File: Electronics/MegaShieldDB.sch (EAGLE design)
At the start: 45 parts, among them IC2 MCP4802, IC3 MCP4802, IC4 4013N, Q1 BF199, Q5 BF199, X1 Panel, X2 Cruise, X3 Motor, X4 Steer, X5 Brake

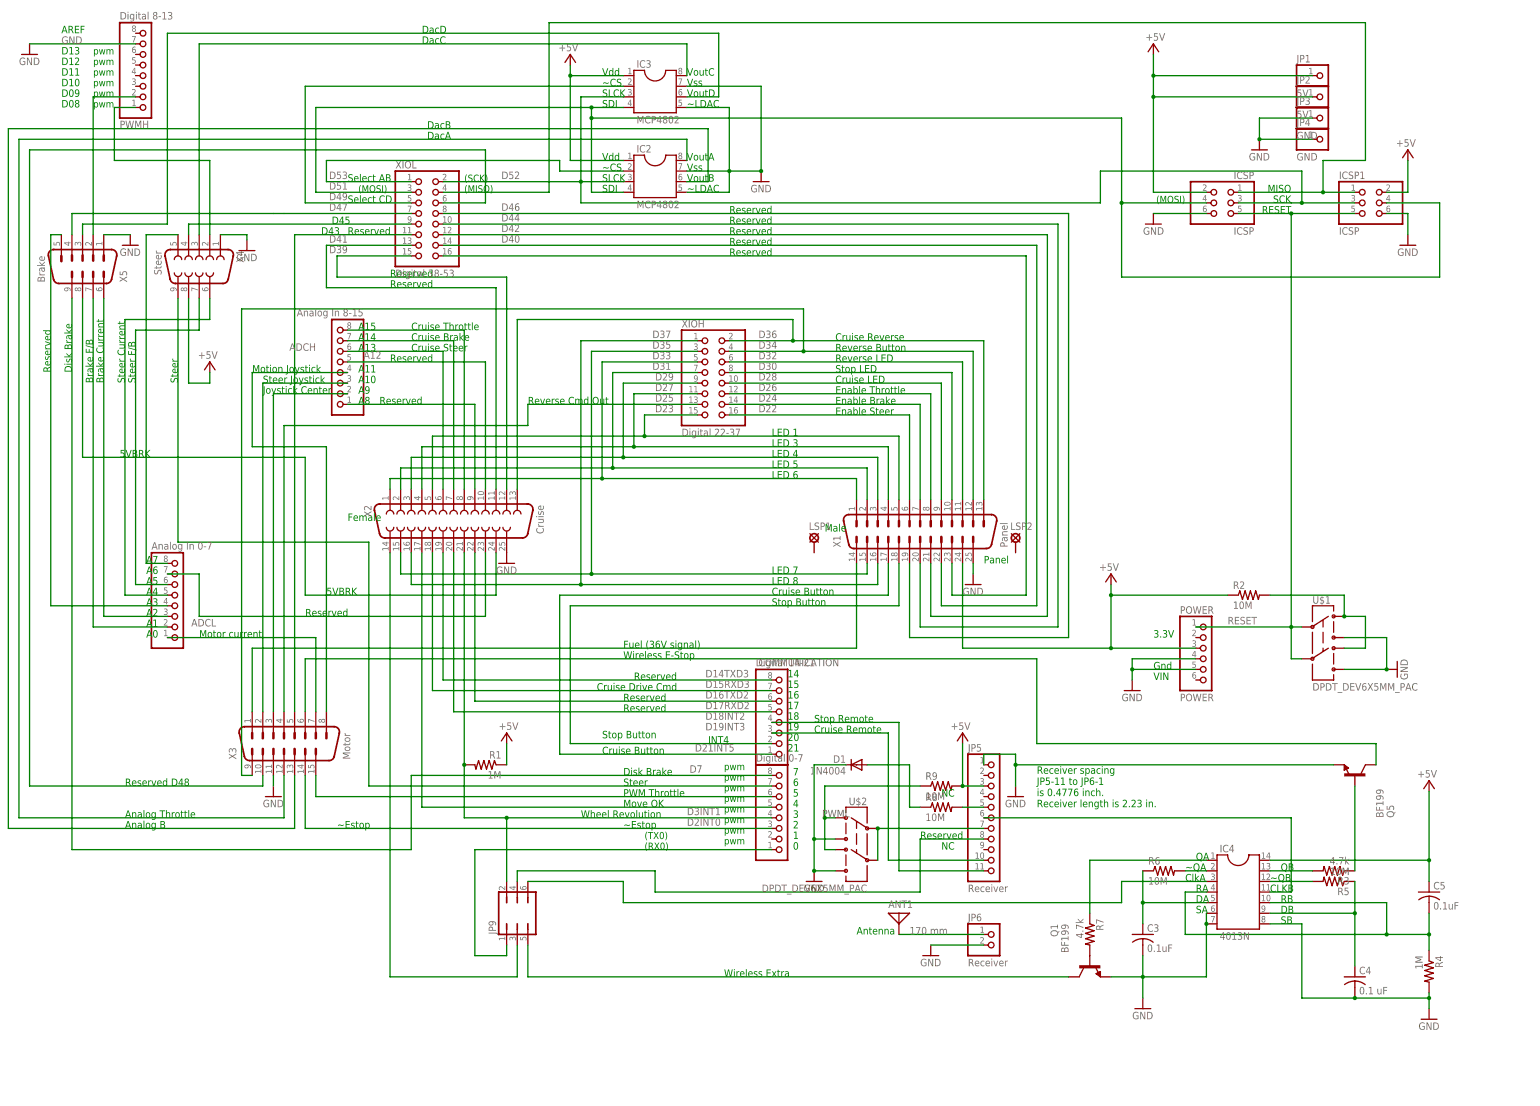
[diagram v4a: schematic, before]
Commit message: Routed with thick power and ground.
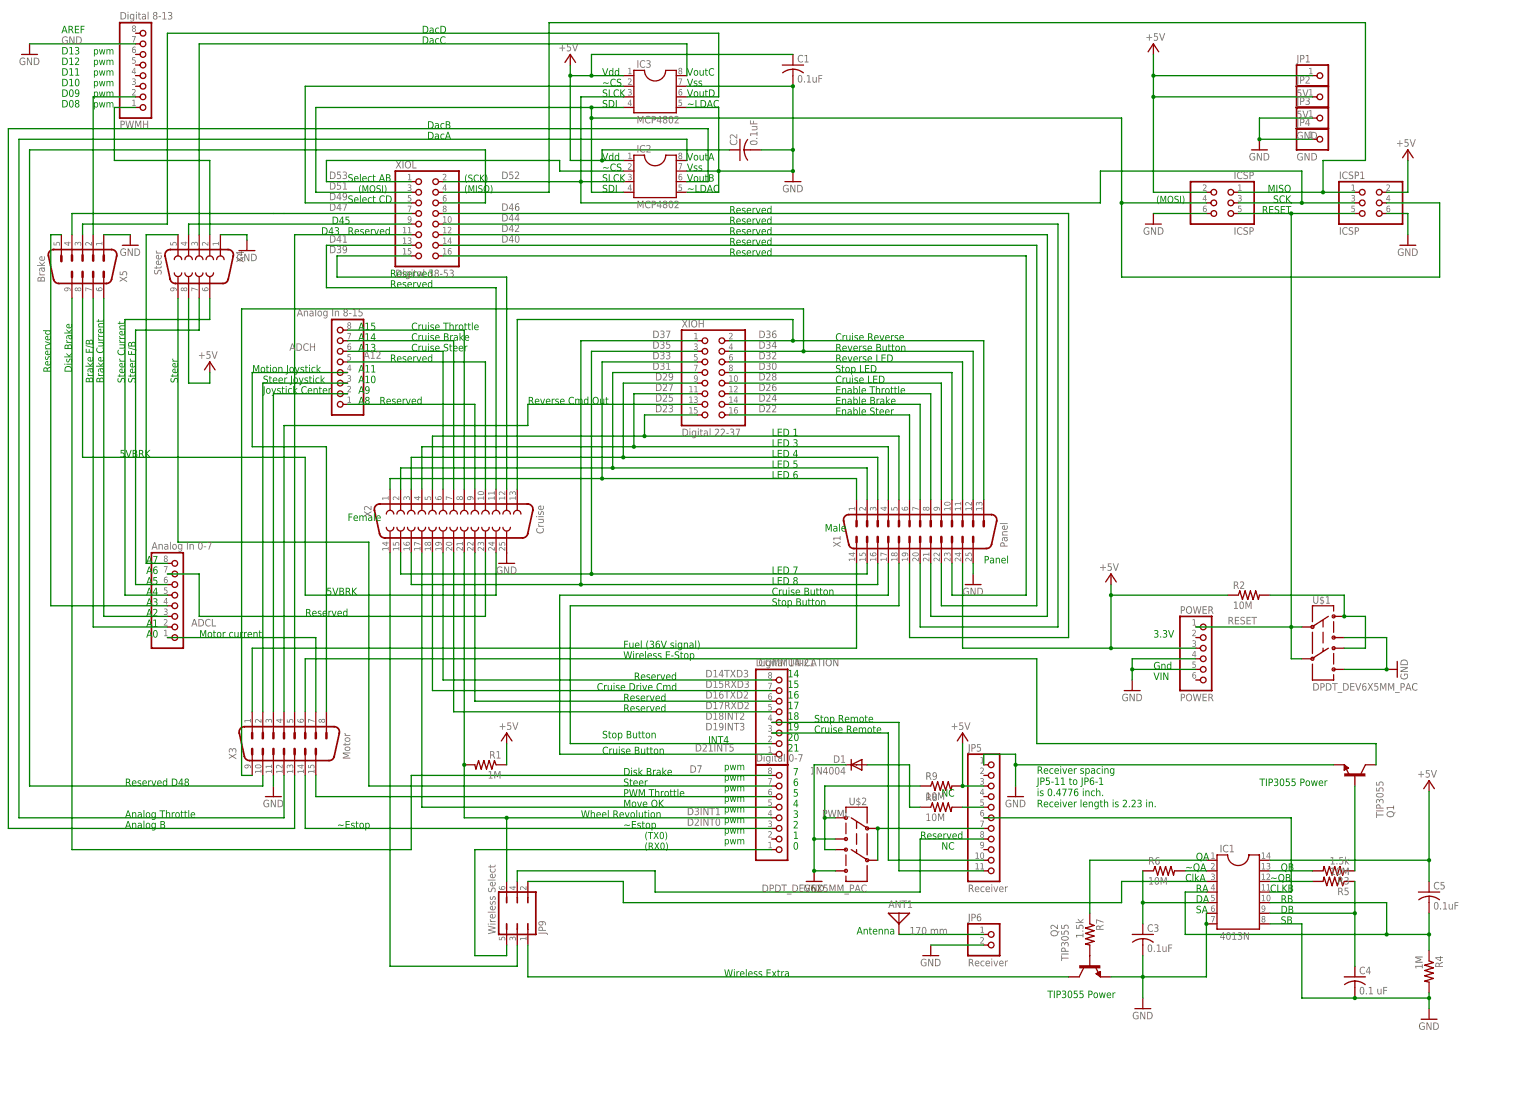
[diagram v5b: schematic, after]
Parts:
- removed LSP1, LSP2: LSP13, solpad:LSP13
- removed Q5: BF199, transistor-npn:BF199
- added C1, C2: 0.1uF, rcl:C-US025-025X050
- added Q2: TIP3055, transistor-neu-to92:BD535
- JP9: value (none) -> Wireless Select
- Q1: value BF199 -> TIP3055; device transistor-npn:BF199 -> transistor-neu-to92:BD535
- R3, R7: value 4.7k -> 1.5k
- renumbered IC4 to IC1
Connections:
- removed net N$12: Q1.B, R7.2
- new net N$3: Q2.B, R7.2
- net +5V: now also C1.1, C2.1
- net CLKA: now also JP9.2; no longer JP9.6
- net D0RX0: now also JP9.5; no longer JP9.1
- net D3INT1: now also JP9.6; no longer JP9.2
- net GND: now also C1.2, C2.2, Q2.E; no longer Q5.E
- net N$33: now also Q1.B; no longer Q5.B
- net WLES: now also Q1.C; no longer Q5.C
- net WLXCOLL: now also JP9.1, Q2.C; no longer JP9.5, Q1.C
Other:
- note added: "TIP3055 Power"
- moved on the sheet: Q1

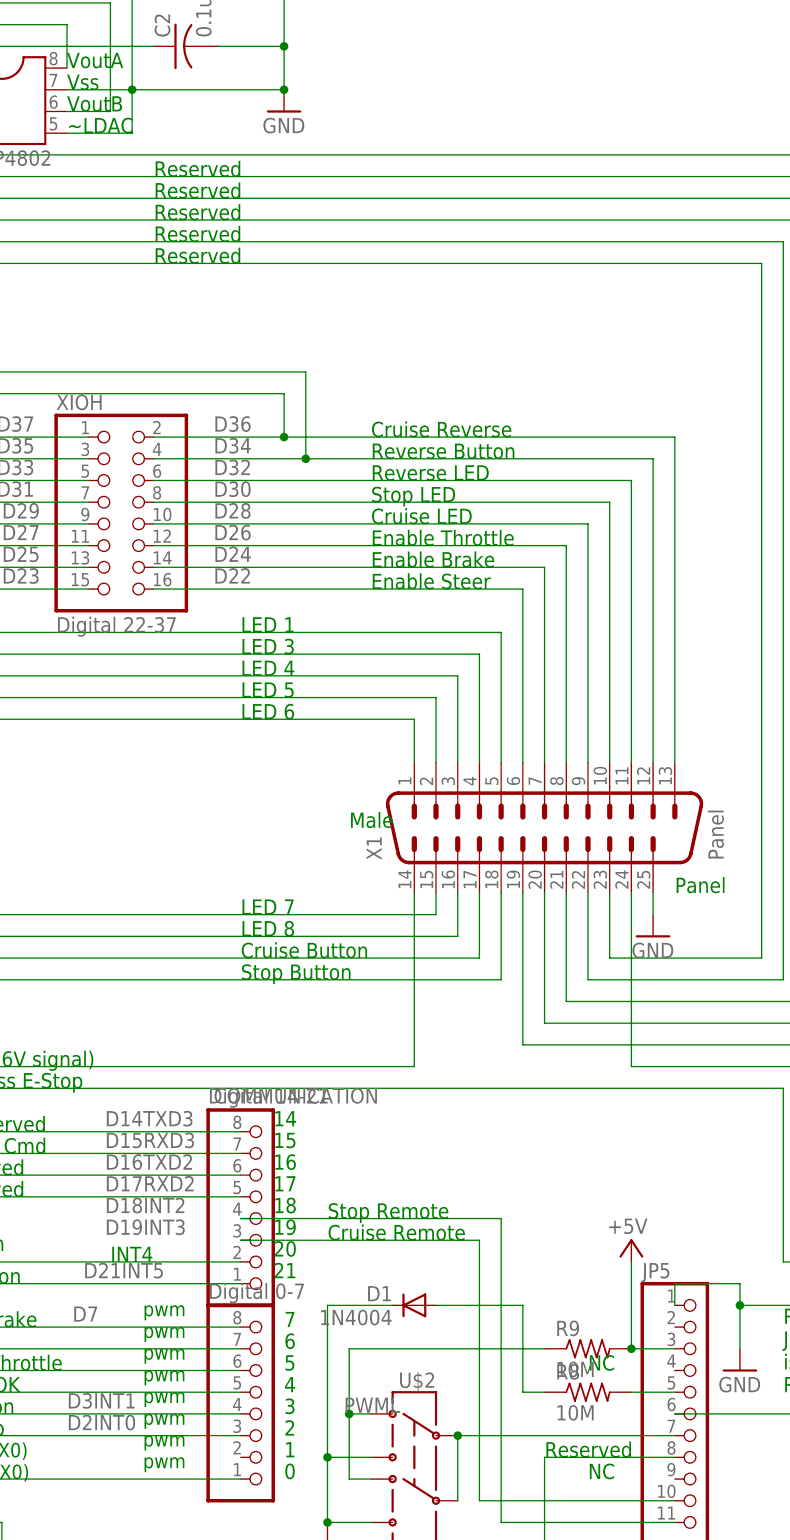
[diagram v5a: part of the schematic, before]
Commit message: 3 new boards
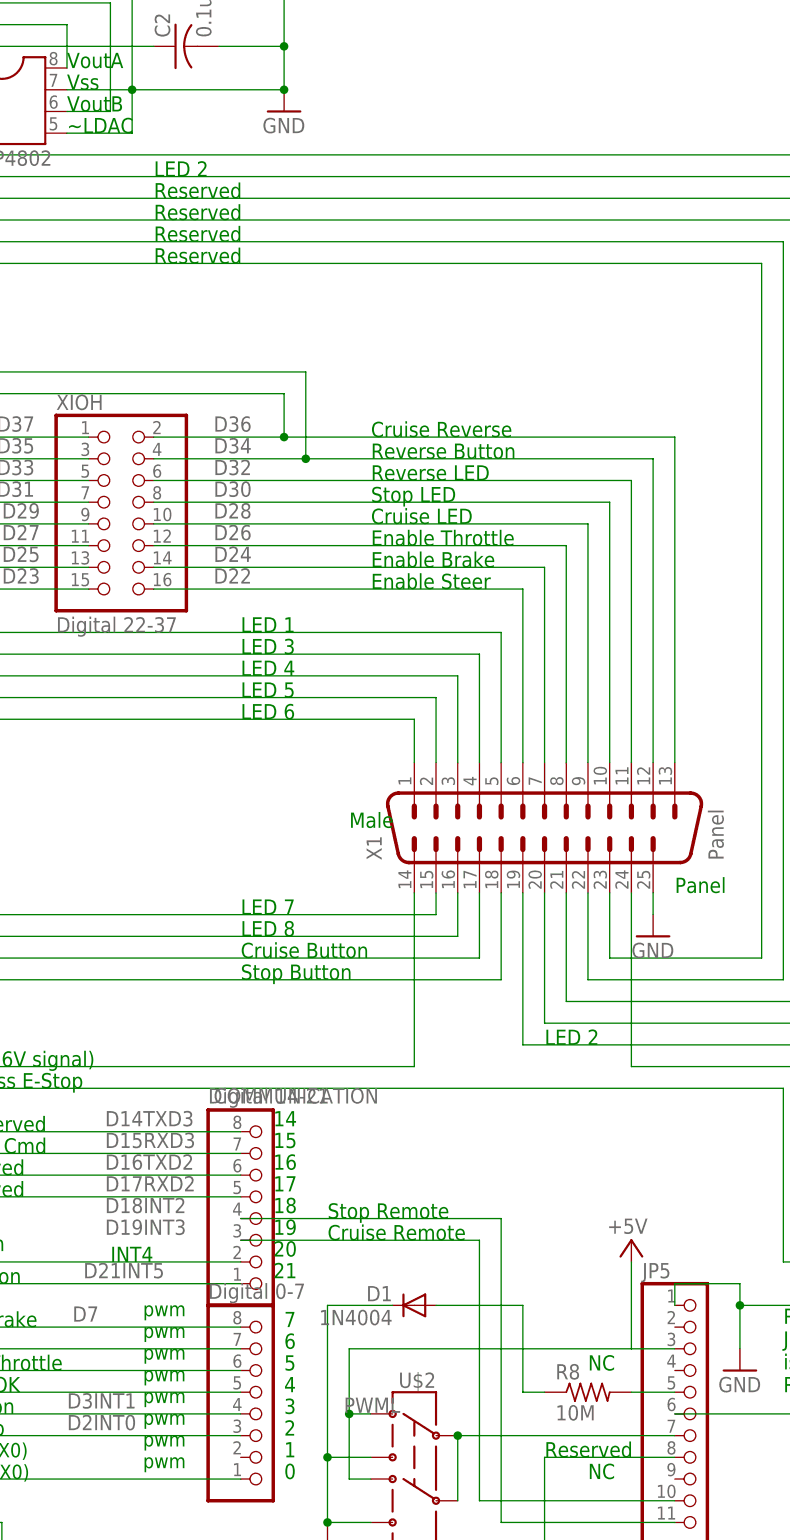
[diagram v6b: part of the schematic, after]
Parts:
- removed R9: 10M, rcl:R-US_0204/5
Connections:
- removed net N$10: R9.1, U$2.1, U$2.4
- net +5V: now also U$2.1, U$2.4; no longer R9.2
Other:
- note added: "LED 2"
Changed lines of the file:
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@@
 <part name="P+7" library="supply1" deviceset="+5V" device=""/>
 <part name="R2" library="rcl" deviceset="R-US_" device="0204/5" value="10M"/>
-<part name="R9" library="rcl" deviceset="R-US_" device="0204/5" value="10M"/>
 <part name="X3" library="con-subd" deviceset="M15" device="-182" value="Motor"/>
 <part name="U$1" library="elcanoParts" deviceset="DPDT_DEV" device="6X5MM_PAC"/>
@@
 <text x="93.98" y="68.58" size="1.778" layer="91">Reserved</text>
 <text x="15.24" y="83.82" size="1.778" layer="91">Reserved</text>
-<text x="116.84" y="180.34" size="1.778" layer="91">Reserved</text>
 <text x="116.84" y="177.8" size="1.778" layer="91">Reserved</text>
 <text x="116.84" y="175.26" size="1.778" layer="91">Reserved</text>
@@
 <text x="243.84" y="43.18" size="1.778" layer="91">TIP3055 Power</text>
 <text x="193.04" y="-7.62" size="1.778" layer="91">TIP3055 Power</text>
+<text x="116.84" y="180.34" size="1.778" layer="91">LED 2</text>
+<text x="162.56" y="78.74" size="1.778" layer="91">LED 2</text>
 </plain>
 <instances>
@@
 </instance>
 <instance part="R2" gate="G$1" x="241.3" y="88.9"/>
-<instance part="R9" gate="G$1" x="167.64" y="43.18"/>
 <instance part="X3" gate="-1" x="10.16" y="53.34" rot="R90"/>
 <instance part="U$1" gate="G$1" x="259.08" y="78.74"/>
@@
 <wire x1="177.8" y1="43.18" x2="172.72" y2="43.18" width="0.1524" layer="91"/>
 <wire x1="172.72" y1="43.18" x2="172.72" y2="53.34" width="0.1524" layer="91"/>
-<junction x="172.72" y="43.18"/>
-<pinref part="R9" gate="G$1" pin="2"/>
+<wire x1="172.72" y1="43.18" x2="139.7" y2="43.18" width="0.1524" layer="91"/>
+<wire x1="139.7" y1="43.18" x2="139.7" y2="35.56" width="0.1524" layer="91"/>
+<pinref part="U$2" gate="G$1" pin="1"/>
+<wire x1="142.24" y1="35.56" x2="139.7" y2="35.56" width="0.1524" layer="91"/>
+<wire x1="139.7" y1="35.56" x2="139.7" y2="27.94" width="0.1524" layer="91"/>
+<pinref part="U$2" gate="G$1" pin="4"/>
+<wire x1="139.7" y1="27.94" x2="142.24" y2="27.94" width="0.1524" layer="91"/>
+<junction x="139.7" y="35.56"/>
 </segment>
 <segment>
@@
 </segment>
 </net>
-<net name="N$10" class="0">
-<segment>
-<pinref part="R9" gate="G$1" pin="1"/>
-<wire x1="162.56" y1="43.18" x2="139.7" y2="43.18" width="0.1524" layer="91"/>
-<wire x1="139.7" y1="43.18" x2="139.7" y2="35.56" width="0.1524" layer="91"/>
-<pinref part="U$2" gate="G$1" pin="1"/>
-<wire x1="142.24" y1="35.56" x2="139.7" y2="35.56" width="0.1524" layer="91"/>
-<wire x1="139.7" y1="35.56" x2="139.7" y2="27.94" width="0.1524" layer="91"/>
-<pinref part="U$2" gate="G$1" pin="4"/>
-<wire x1="139.7" y1="27.94" x2="142.24" y2="27.94" width="0.1524" layer="91"/>
-<junction x="139.7" y="35.56"/>
-</segment>
-</net>

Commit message: Corrected Base/Emitteron Q1, Q2
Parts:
- Q1, Q2: device transistor-neu-to92:BD535 -> transistor-neu-to92:BD239
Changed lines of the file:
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@@
 <part name="U$2" library="elcanoParts" deviceset="DPDT_DEV" device="6X5MM_PAC"/>
 <part name="JP9" library="jumper" deviceset="JP3Q" device="" value="Wireless Select"/>
-<part name="Q1" library="transistor-neu-to92" deviceset="BD535" device="" value="TIP3055"/>
-<part name="Q2" library="transistor-neu-to92" deviceset="BD535" device="" value="TIP3055"/>
+<part name="Q1" library="transistor-neu-to92" deviceset="BD239" device="" value="TIP3055"/>
+<part name="Q2" library="transistor-neu-to92" deviceset="BD239" device="" value="TIP3055"/>
 <part name="C1" library="rcl" deviceset="C-US" device="025-025X050" value="0.1uF"/>
 <part name="C2" library="rcl" deviceset="C-US" device="025-025X050" value="0.1uF"/>
